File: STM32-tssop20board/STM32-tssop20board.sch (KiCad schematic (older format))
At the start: 23 parts, among them J1 Conn_01x10_Male, J2 Conn_01x10_Male, J3 Conn_01x03_Male, J4 USB_A, J5 USB_B_Micro, J6 Target_SWD, J7 IF_SWD, J8 Target_UART, SW1 Reset, U1 STM32F042F6Px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

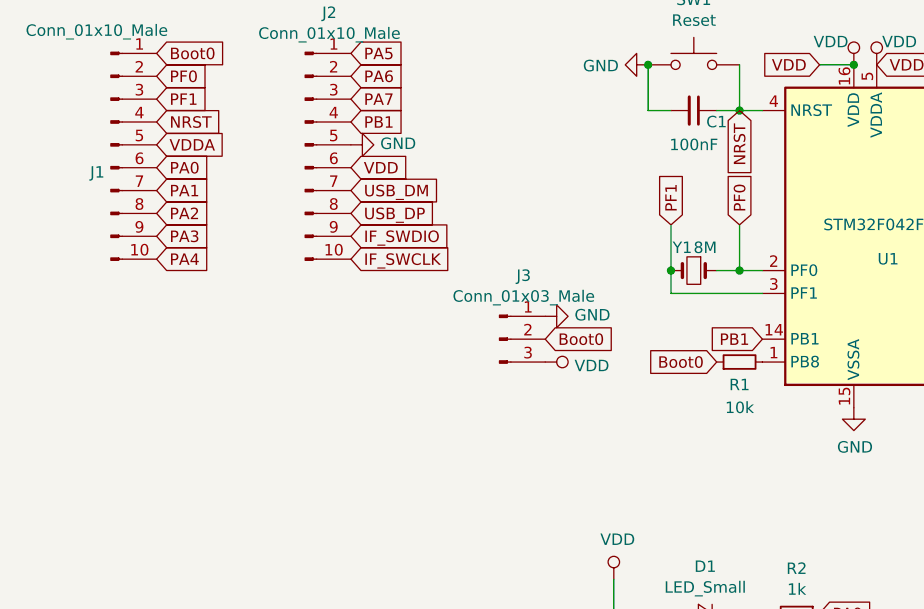
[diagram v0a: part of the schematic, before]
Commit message: stm32-tssop20board: Fix capacitor for oscillator
Signed-off-by: Zamir SUN <sztsian@gmail.com>
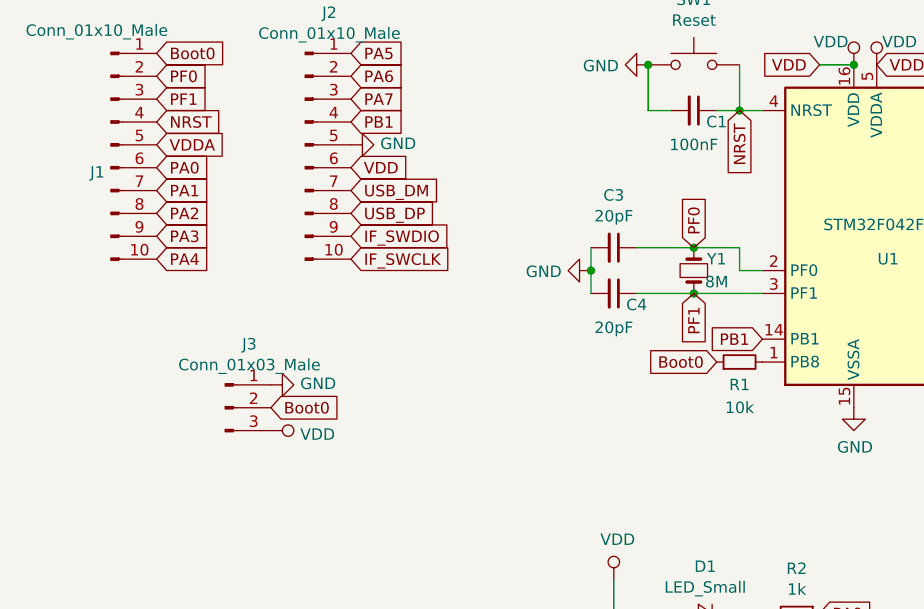
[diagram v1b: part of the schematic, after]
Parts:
- added C3, C4: 20pF, Capacitor_SMD:C_0805_2012Metric_Pad1.15x1.40mm_HandSolder, symbol Device:C_Small
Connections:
- net GND: now also C3.2, C4.2
- net PF0: now also Y1.2, C3.1; no longer Y1.1
- net PF1: now also Y1.1, C4.1; no longer Y1.2
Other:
- moved on the sheet: J3
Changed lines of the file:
@@
 EESchema Schematic File Version 4
 LIBS:STM32-tssop20board-cache
-EELAYER 26 0
+EELAYER 29 0
 EELAYER END
 $Descr A4 11693 8268
@@
 L Connector:Conn_01x03_Male J3
 U 1 1 5CA17AC9
-P 2850 2200
-F 0 "J3" H 2956 2478 50  0000 C CNN
-F 1 "Conn_01x03_Male" H 2956 2387 50  0000 C CNN
-F 2 "Connector_PinHeader_2.54mm:PinHeader_1x03_P2.54mm_Vertical" H 2850 2200 50  0001 C CNN
-F 3 "~" H 2850 2200 50  0001 C CNN
-	1    2850 2200
+P 1650 2500
+F 0 "J3" H 1756 2778 50  0000 C CNN
+F 1 "Conn_01x03_Male" H 1756 2687 50  0000 C CNN
+F 2 "Connector_PinHeader_2.54mm:PinHeader_1x03_P2.54mm_Vertical" H 1650 2500 50  0001 C CNN
+F 3 "~" H 1650 2500 50  0001 C CNN
+	1    1650 2500
 	1    0    0    -1
 $EndComp
@@
 Text GLabel 3800 2300 0    50   Input ~ 0
 Boot0
-Text GLabel 3050 2200 2    50   Input ~ 0
+Text GLabel 1850 2500 2    50   Input ~ 0
 Boot0
 $Comp
 L power:GND #PWR02
 U 1 1 5CA17D4F
-P 3050 2100
-F 0 "#PWR02" H 3050 1850 50  0001 C CNN
-F 1 "GND" V 3055 1972 50  0000 R CNN
-F 2 "" H 3050 2100 50  0001 C CNN
-F 3 "" H 3050 2100 50  0001 C CNN
-	1    3050 2100
+P 1850 2400
+F 0 "#PWR02" H 1850 2150 50  0001 C CNN
+F 1 "GND" V 1855 2272 50  0000 R CNN
+F 2 "" H 1850 2400 50  0001 C CNN
+F 3 "" H 1850 2400 50  0001 C CNN
+	1    1850 2400
 	0    -1   -1   0
 $EndComp
@@
 L power:VDD #PWR03
 U 1 1 5CA17DC8
-P 3050 2300
-F 0 "#PWR03" H 3050 2150 50  0001 C CNN
-F 1 "VDD" V 3067 2428 50  0000 L CNN
-F 2 "" H 3050 2300 50  0001 C CNN
-F 3 "" H 3050 2300 50  0001 C CNN
-	1    3050 2300
+P 1850 2600
+F 0 "#PWR03" H 1850 2450 50  0001 C CNN
+F 1 "VDD" V 1867 2728 50  0000 L CNN
+F 2 "" H 1850 2600 50  0001 C CNN
+F 3 "" H 1850 2600 50  0001 C CNN
+	1    1850 2600
 	0    1    1    0
 $EndComp
@@
 U 1 1 5CA18233
 P 3700 1900
-F 0 "Y1" H 3750 1800 50  0000 C CNN
-F 1 "8M" H 3650 1800 50  0000 C CNN
+F 0 "Y1" V 3750 1800 50  0000 C CNN
+F 1 "8M" V 3650 1800 50  0000 C CNN
 F 2 "Crystal:Crystal_SMD_5032-2Pin_5.0x3.2mm_HandSoldering" H 3700 1900 50  0001 C CNN
 F 3 "~" H 3700 1900 50  0001 C CNN
 	1    3700 1900
-	-1   0    0    1
-$EndComp
-Wire Wire Line
-	4000 1900 3900 1900
-Wire Wire Line
-	4000 2000 3600 2000
-Wire Wire Line
-	3600 2000 3600 1900
-Text GLabel 3600 1700 1    50   Input ~ 0
+	0    -1   -1   0
+$EndComp
+Wire Wire Line
+	4000 2000 3700 2000
+Text GLabel 3700 2000 3    50   Input ~ 0
 PF1
-Text GLabel 3900 1700 1    50   Input ~ 0
+Text GLabel 3700 1800 1    50   Input ~ 0
 PF0
-Wire Wire Line
-	3600 1900 3600 1700
-Connection ~ 3600 1900
-Wire Wire Line
-	3900 1700 3900 1900
-Connection ~ 3900 1900
-Wire Wire Line
-	3900 1900 3800 1900
 $Comp
 L Device:C_Small C1
@@
 	7950 1100 7650 1100
 Connection ~ 7650 1100
+Connection ~ 3700 2000
+Wire Wire Line
+	4000 1900 3900 1900
+Wire Wire Line
+	3900 1900 3900 1800
+Wire Wire Line
+	3900 1800 3700 1800
+$Comp
+L power:GND #PWR021
+U 1 1 5CF21CAF
+P 3250 1900
+F 0 "#PWR021" H 3250 1650 50  0001 C CNN
+F 1 "GND" V 3255 1772 50  0000 R CNN
+F 2 "" H 3250 1900 50  0001 C CNN
+F 3 "" H 3250 1900 50  0001 C CNN
+	1    3250 1900
+	0    1    1    0
+$EndComp
+$Comp
+L Device:C_Small C3
+U 1 1 5CF225FD
+P 3350 1800
+F 0 "C3" V 3121 1800 50  0000 C CNN
+F 1 "20pF" V 3212 1800 50  0000 C CNN
+F 2 "Capacitor_SMD:C_0805_2012Metric_Pad1.15x1.40mm_HandSolder" H 3350 1800 50  0001 C CNN
+F 3 "~" H 3350 1800 50  0001 C CNN
+	1    3350 1800
+	0    1    1    0
+$EndComp
+$Comp
+L Device:C_Small C4
+U 1 1 5CF2309D
+P 3350 2000
+F 0 "C4" V 3400 2100 50  0000 C CNN
+F 1 "20pF" V 3500 2000 50  0000 C CNN
+F 2 "Capacitor_SMD:C_0805_2012Metric_Pad1.15x1.40mm_HandSolder" H 3350 2000 50  0001 C CNN
+F 3 "~" H 3350 2000 50  0001 C CNN
+	1    3350 2000
+	0    1    1    0
+$EndComp
+Wire Wire Line
+	3450 2000 3700 2000
+Wire Wire Line
+	3450 1800 3700 1800
+Connection ~ 3700 1800
+Wire Wire Line
+	3250 1800 3250 1900
+Wire Wire Line
+	3250 1900 3250 2000
+Connection ~ 3250 1900
 $EndSCHEMATC
